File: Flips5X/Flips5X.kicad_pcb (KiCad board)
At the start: 2 copper layers, 100 x 100 mm, 19 parts, among them CN1 Conn_02x30_Odd_Even, CN2 UFP2810, CN3 UFP2810, U1 FP2800A, U2 FP2800A, U3 FP2800A

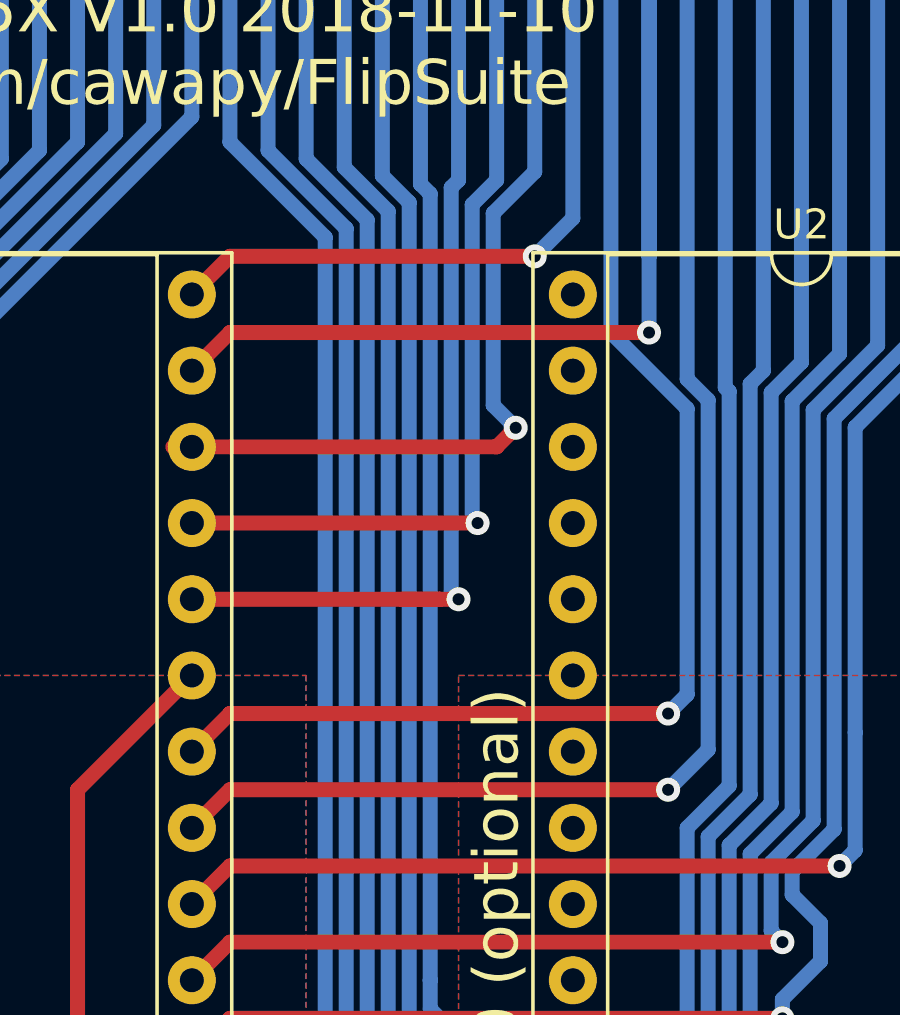
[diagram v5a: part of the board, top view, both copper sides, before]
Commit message: less fragmented GND planes
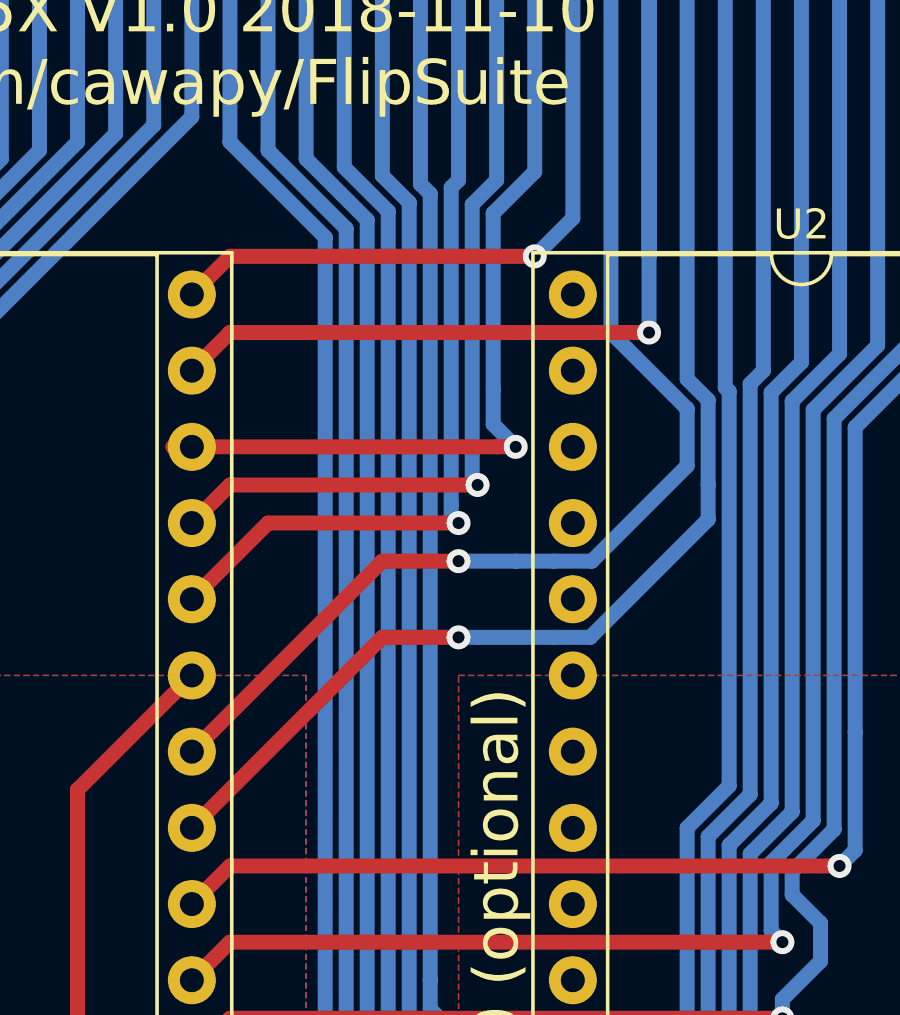
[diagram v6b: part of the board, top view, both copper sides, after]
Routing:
- net /RY5: track 75.2 -> 59.3 mm
- net /RY7: track 66.2 -> 61.7 mm
- net /RY1: track 53.6 -> 50.9 mm
- net /RY2: track 50.1 -> 49.4 mm

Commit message: minor retracing
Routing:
- net /RY4: track 42.7 -> 43.4 mm
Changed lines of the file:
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@@
     (thickness 1.6)
     (drawings 110)
-    (tracks 641)
+    (tracks 646)
     (zones 0)
     (modules 19)
@@
   (segment (start 92.71 57.15) (end 92.71 66.04) (width 0.5) (layer B.Cu) (net 82) (status 800020))
   (segment (start 92.71 66.04) (end 92.71 66.675) (width 0.5) (layer B.Cu) (net 82) (status C00030))
+  (segment (start 92.075 84.455) (end 92.71 85.09) (width 0.5) (layer B.Cu) (net 82))
+  (segment (start 93.98 81.989904) (end 92.025063 83.944841) (width 0.5) (layer B.Cu) (net 82))
+  (segment (start 93.98 81.915) (end 93.98 81.989904) (width 0.5) (layer B.Cu) (net 82))
+  (segment (start 93.98 67.945) (end 93.98 81.915) (width 0.5) (layer B.Cu) (net 82))
   (segment (start 92.71 66.675) (end 93.98 67.945) (width 0.5) (layer B.Cu) (net 82) (status 400010))
-  (segment (start 93.98 67.945) (end 93.98 83.82) (width 0.5) (layer B.Cu) (net 82))
   (segment (start 81.28 86.36) (end 82.55 85.09) (width 0.5) (layer F.Cu) (net 82) (status 400010))
-  (segment (start 92.71 85.09) (end 93.98 83.82) (width 0.5) (layer B.Cu) (net 82))
+  (segment (start 82.55 85.09) (end 92.71 85.09) (width 0.5) (layer F.Cu) (net 82))
   (via (at 92.71 85.09) (size 0.8) (drill 0.4) (layers F.Cu B.Cu) (net 82))
-  (segment (start 82.55 85.09) (end 92.71 85.09) (width 0.5) (layer F.Cu) (net 82))
+  (segment (start 92.660063 85.09) (end 92.71 85.09) (width 0.5) (layer B.Cu) (net 82))
+  (segment (start 92.075 84.455) (end 92.025063 84.405063) (width 0.5) (layer B.Cu) (net 82))
+  (segment (start 92.025063 84.405063) (end 92.025063 83.944841) (width 0.5) (layer B.Cu) (net 82))
   (segment (start 93.98 55.88) (end 95.25 57.15) (width 0.5) (layer B.Cu) (net 83) (status 400010))
   (segment (start 95.25 64.135) (end 95.25 57.15) (width 0.5) (layer B.Cu) (net 83))

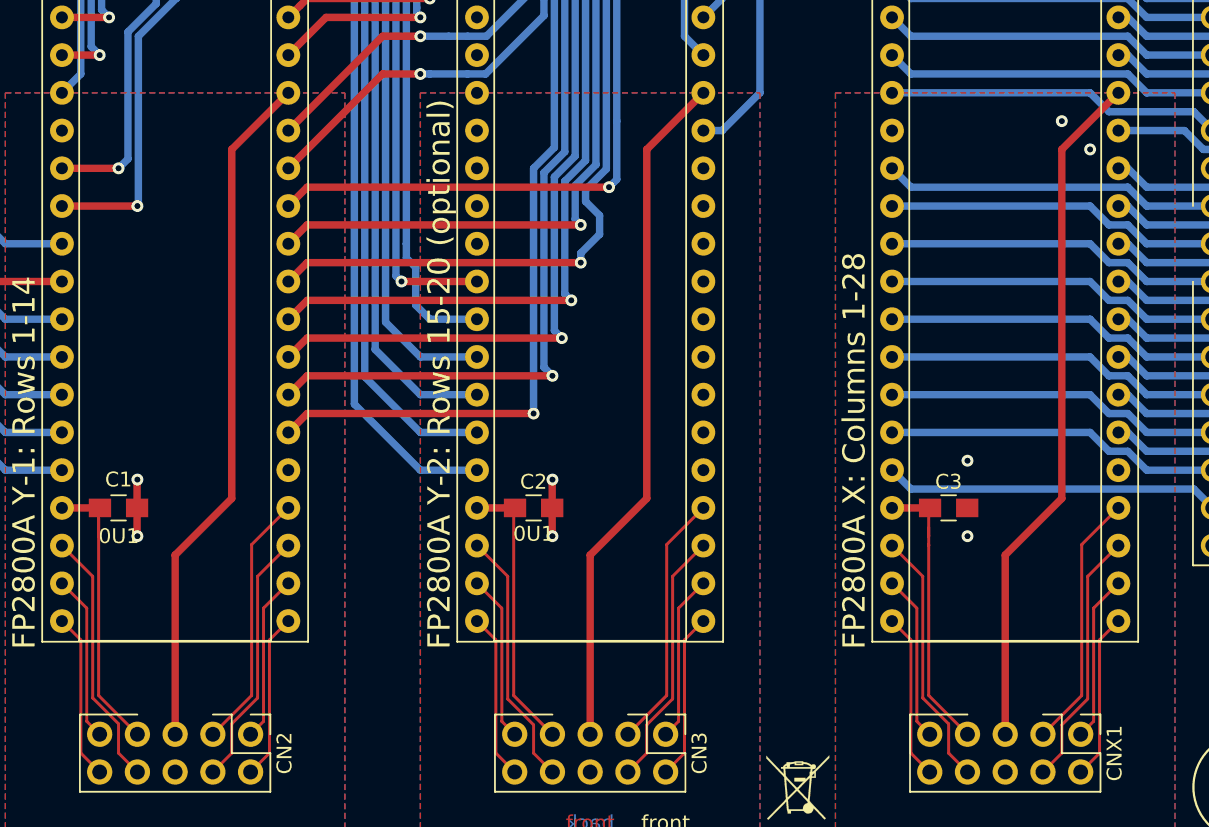
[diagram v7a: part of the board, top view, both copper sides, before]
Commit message: adding R3 and 0μ1 value to PCB, including FP2800 values
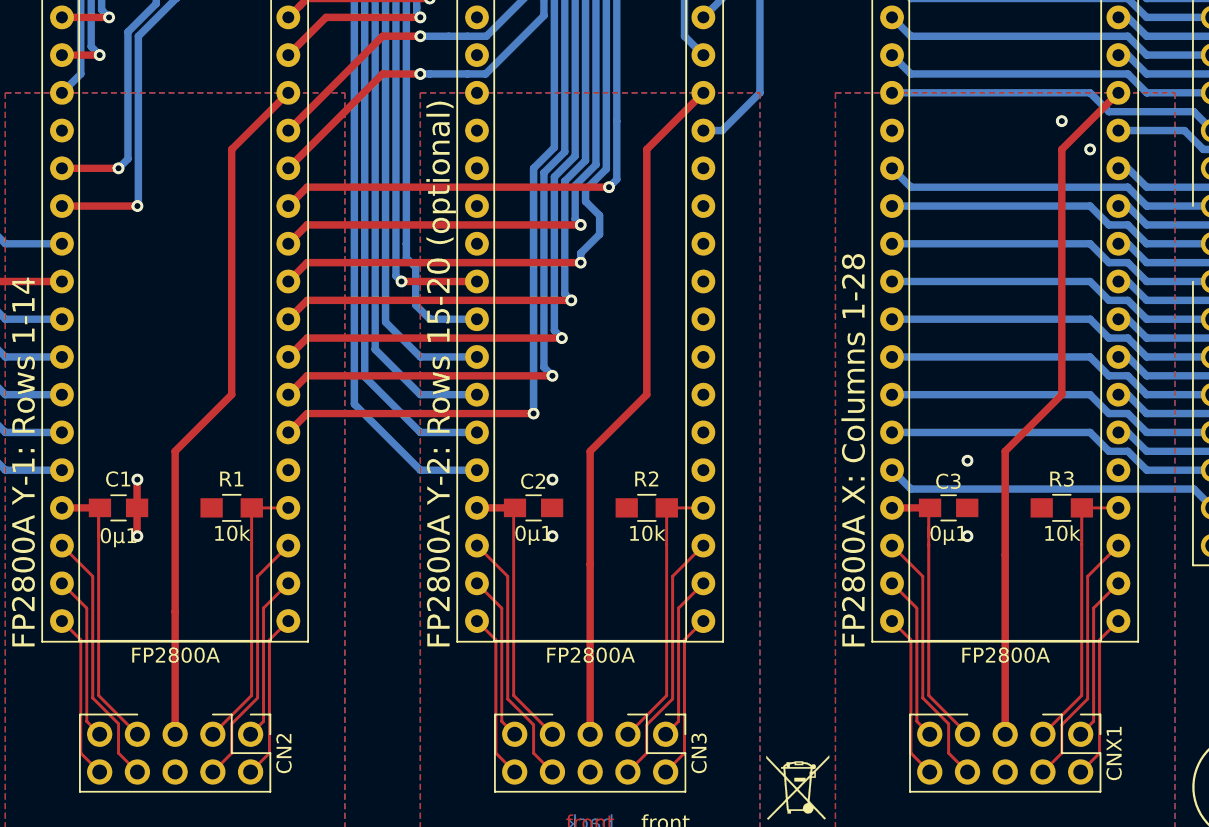
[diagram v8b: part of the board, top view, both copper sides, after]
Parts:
- added R1: 10k, Resistors_SMD:R_0805_HandSoldering, F.Cu at (77.5, 127.0)
- added R2: 10k, Resistors_SMD:R_0805_HandSoldering, F.Cu at (105.4, 127.0)
- added R3: 10k, Resistors_SMD:R_0805_HandSoldering, F.Cu at (133.3, 127.0)
- C1, C2, C3: value 0U1 -> 0μ1
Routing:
- net /R.GND: track 3.83 -> 0.06 mm
- net /X.EN: track 17.3 -> 18.8 mm
- net /R.EN: track 17.3 -> 18.8 mm
- net /L.EN: track 17.3 -> 18.8 mm
